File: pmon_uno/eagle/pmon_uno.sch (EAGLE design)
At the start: 42 parts, among them J1 USB, J2 USB, J3 PINHD-1X3, J4 PINHD-2X3, Q1 16Mhz, U1 LTC2943, U2 FT232RL, U3 LT1764AEQ, U4 ATMEGA328TQFP32

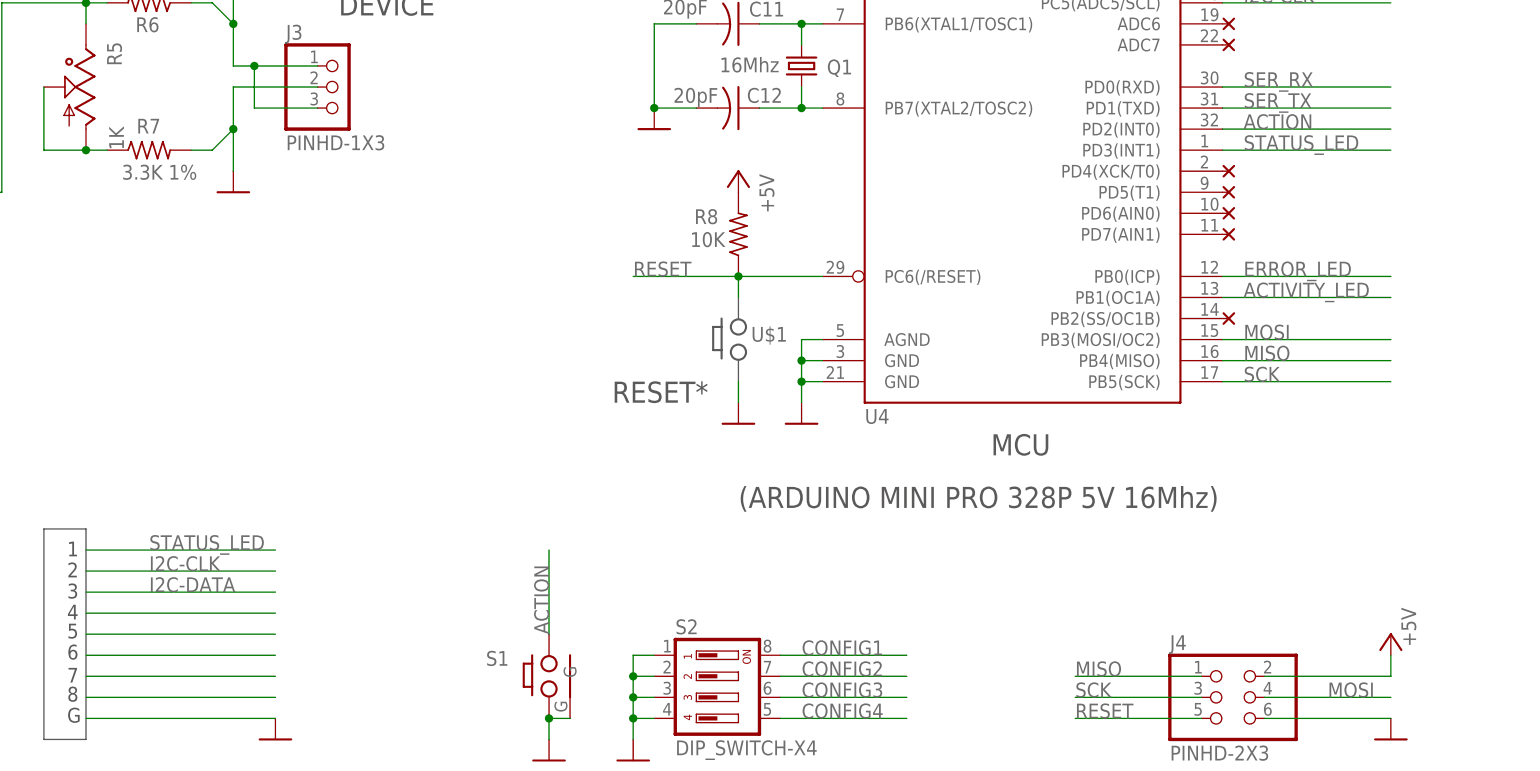
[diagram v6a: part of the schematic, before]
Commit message: Minor Eagle tweaks: 1. Added a debug pin to the logic analyzer signals. 2. Changed the top and bottom drill sizes from 2.5mm to 3mm.
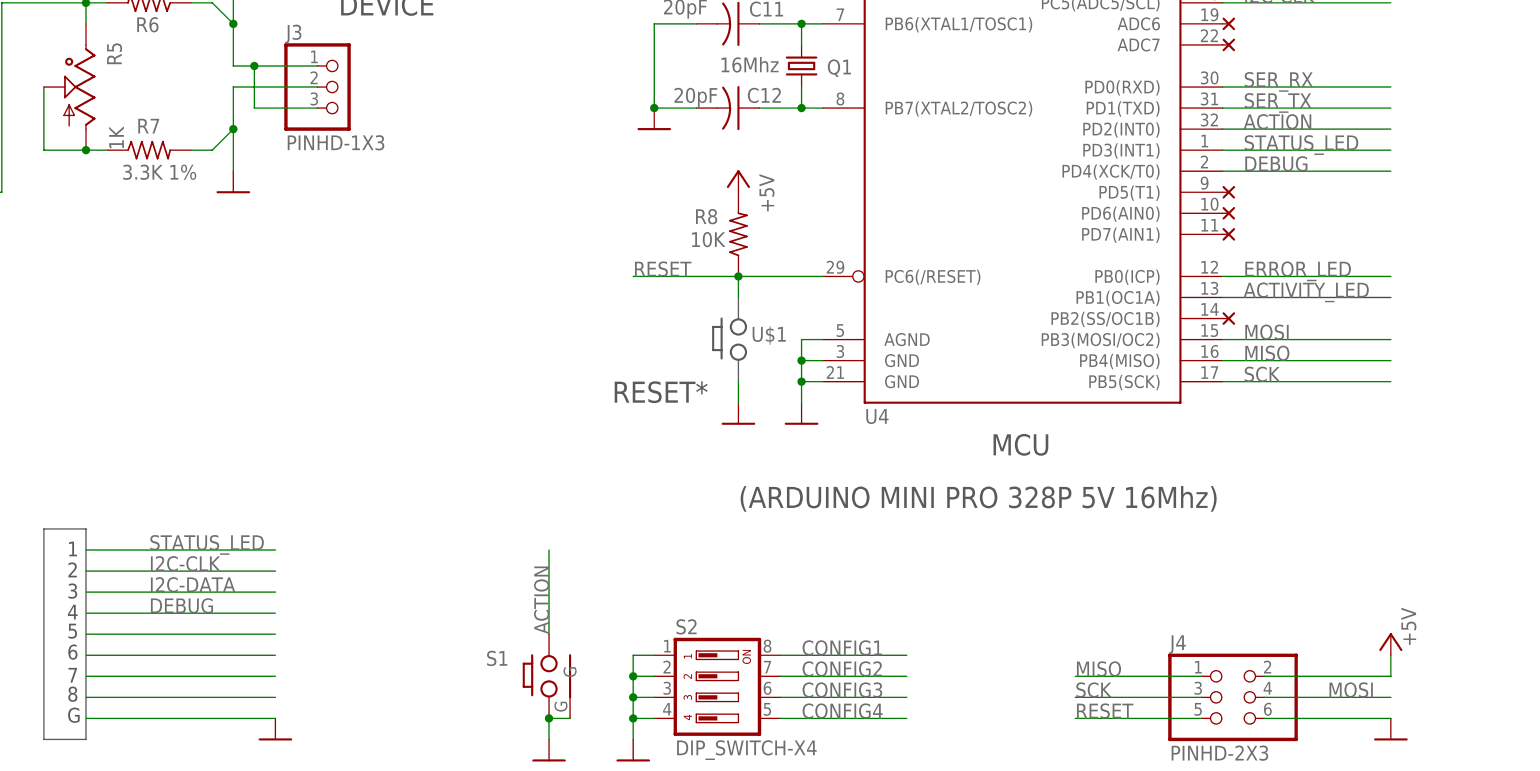
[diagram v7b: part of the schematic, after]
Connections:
- new net DEBUG: U4.PD4(XCK/T0)
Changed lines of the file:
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@@
 <part name="U$11" library="pmon_uno" deviceset="NC" device=""/>
 <part name="U$12" library="pmon_uno" deviceset="NC" device=""/>
-<part name="U$14" library="pmon_uno" deviceset="NC" device=""/>
 <part name="U$16" library="pmon_uno" deviceset="NC" device=""/>
 <part name="U$18" library="pmon_uno" deviceset="NC" device=""/>
@@
 <instance part="U$11" gate="G$1" x="238.76" y="198.12" rot="R180"/>
 <instance part="U$12" gate="G$1" x="238.76" y="195.58" rot="R180"/>
-<instance part="U$14" gate="G$1" x="238.76" y="180.34" rot="R180"/>
 <instance part="U$16" gate="G$1" x="238.76" y="177.8" rot="R180"/>
 <instance part="U$18" gate="G$1" x="238.76" y="172.72" rot="R180"/>
@@
 </segment>
 </net>
-<net name="N$5" class="0">
+<net name="N$13" class="0">
+<segment>
+<wire x1="101.6" y1="124.46" x2="124.46" y2="124.46" width="0.1524" layer="91"/>
+</segment>
+</net>
+<net name="N$23" class="0">
+<segment>
+<wire x1="101.6" y1="121.92" x2="124.46" y2="121.92" width="0.1524" layer="91"/>
+</segment>
+</net>
+<net name="N$24" class="0">
+<segment>
+<wire x1="101.6" y1="119.38" x2="124.46" y2="119.38" width="0.1524" layer="91"/>
+</segment>
+</net>
+<net name="N$25" class="0">
+<segment>
+<wire x1="101.6" y1="116.84" x2="124.46" y2="116.84" width="0.1524" layer="91"/>
+</segment>
+</net>
+<net name="DEBUG" class="0">
+<segment>
+<pinref part="U4" gate="G$1" pin="PD4(XCK/T0)"/>
+<wire x1="238.76" y1="180.34" x2="259.08" y2="180.34" width="0.1524" layer="91"/>
+<label x="241.3" y="180.34" size="1.778" layer="95"/>
+</segment>
 <segment>
 <wire x1="101.6" y1="127" x2="124.46" y2="127" width="0.1524" layer="91"/>
-</segment>
-</net>
-<net name="N$13" class="0">
-<segment>
-<wire x1="101.6" y1="124.46" x2="124.46" y2="124.46" width="0.1524" layer="91"/>
-</segment>
-</net>
-<net name="N$23" class="0">
-<segment>
-<wire x1="101.6" y1="121.92" x2="124.46" y2="121.92" width="0.1524" layer="91"/>
-</segment>
-</net>
-<net name="N$24" class="0">
-<segment>
-<wire x1="101.6" y1="119.38" x2="124.46" y2="119.38" width="0.1524" layer="91"/>
-</segment>
-</net>
-<net name="N$25" class="0">
-<segment>
-<wire x1="101.6" y1="116.84" x2="124.46" y2="116.84" width="0.1524" layer="91"/>
-</segment>
-</net>
+<label x="109.22" y="127" size="1.778" layer="95"/>
+</segment>
+</net>

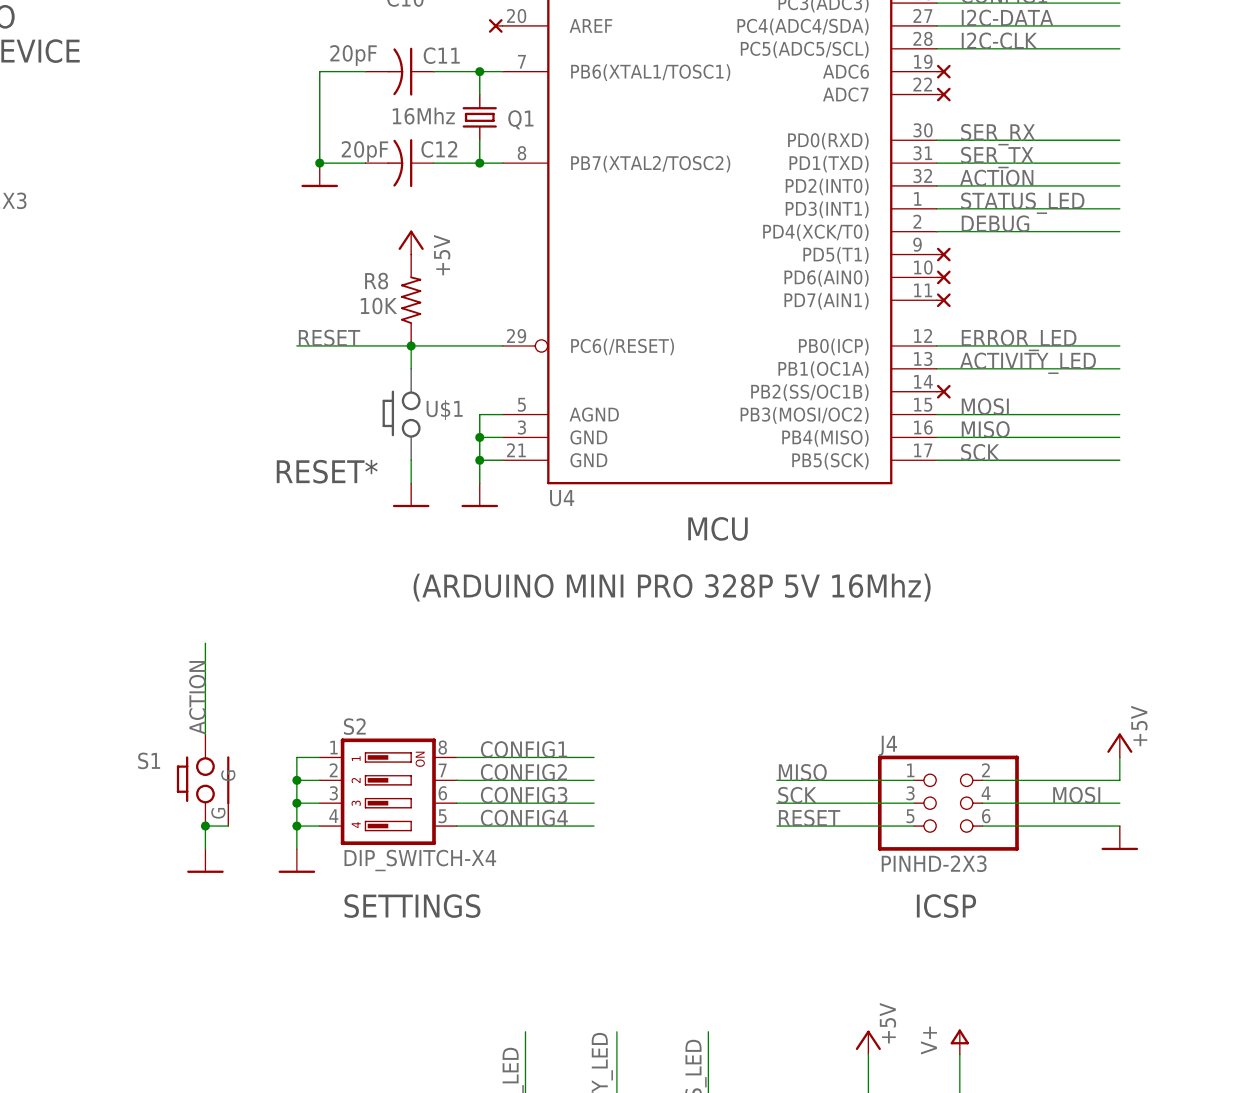
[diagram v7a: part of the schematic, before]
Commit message: Minor text tweaks. No semantic change.
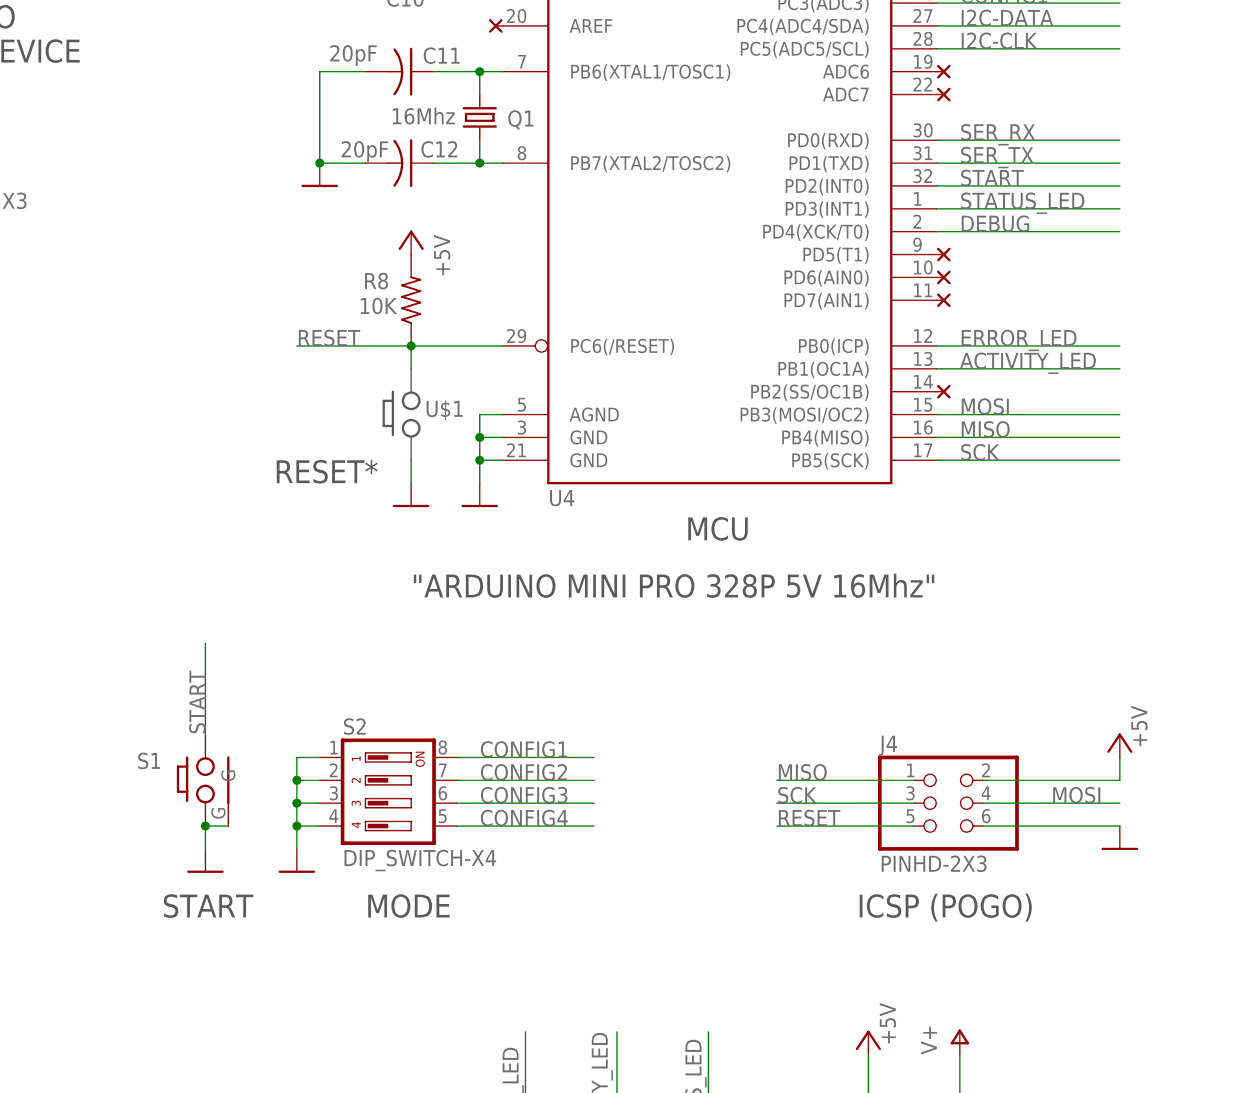
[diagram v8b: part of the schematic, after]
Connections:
- net ACTION renamed START
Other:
- note added: ""ARDUINO MINI PRO 328P 5V 16Mhz""
- note added: "ICSP (POGO)"
- note added: "MODE"
- note added: "START"
- note removed: "(ARDUINO MINI PRO 328P 5V 16Mhz)"
- note removed: "ICSP"
- note removed: "SETTINGS"
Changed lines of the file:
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@@
 <plain>
 <text x="40.64" y="20.32" size="2.54" layer="97">USB/SERIAL</text>
-<text x="236.22" y="104.14" size="2.54" layer="97">ICSP</text>
+<text x="229.87" y="104.14" size="2.54" layer="97">ICSP (POGO)</text>
 <text x="210.82" y="146.05" size="2.54" layer="97">MCU</text>
 <text x="185.42" y="27.94" size="2.54" layer="97" font="vector">Arduino Single Cell Battery Power Monitor</text>
@@
 <text x="132.08" y="199.136" size="2.54" layer="97">TO
 DEVICE</text>
-<text x="172.72" y="104.14" size="2.54" layer="97">SETTINGS</text>
+<text x="175.26" y="104.14" size="2.54" layer="97">MODE</text>
 <text x="102.108" y="213.106" size="2.54" layer="97">3.8V</text>
 <text x="99.314" y="133.858" size="1.778" layer="97">1</text>
@@
 <text x="-25.4" y="7.62" size="2.54" layer="97">* PROTOTYPE ONLY</text>
 <text x="165.1" y="152.4" size="2.54" layer="97">RESET*</text>
-<text x="180.34" y="139.7" size="2.54" layer="97">(ARDUINO MINI PRO 328P 5V 16Mhz)</text>
+<text x="180.34" y="139.7" size="2.54" layer="97">"ARDUINO MINI PRO 328P 5V 16Mhz"</text>
+<text x="152.654" y="104.14" size="2.54" layer="97">START</text>
 </plain>
 <instances>
@@
 </segment>
 </net>
-<net name="ACTION" class="0">
+<net name="START" class="0">
 <segment>
 <wire x1="238.76" y1="185.42" x2="259.08" y2="185.42" width="0.1524" layer="91"/>
